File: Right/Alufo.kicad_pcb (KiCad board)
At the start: 2 copper layers, 139.7 x 88.9 mm, 72 parts, among them J2 USB_C_Receptacle_USB2.0_16P_2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, J4 USB_C_Receptacle_USB2.0_16P_2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, K11 PG1350, K12 PG1350, K13 PG1350, K14 PG1350, K15 PG1350, K16 PG1350, K21 PG1350, K22 PG1350, K23 PG1350, K24 PG1350, K25 PG1350, K26 PG1350, K31 PG1350, K32 PG1350, K33 PG1350, K34 PG1350, K41 PG1350_1½U, K42 PG1350/SKQUCAA010, SW10 BOOT, U2 CH552T, U4 USBLC6-2P6, U6 USBLC6-2P6

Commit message: Update logo and add to PCB
Logo now has PCB revision included and is positioned at top left/right edge ±1.25,+1.25mm.
Author is now positioned between lowest row 2 pad 2 and bottom edge, centred to logo.
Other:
- board text added: "${AUTHOR}"
- board text removed: "${PROJECTNAME} v${PCB_REVISION} • ${AUTHOR}"

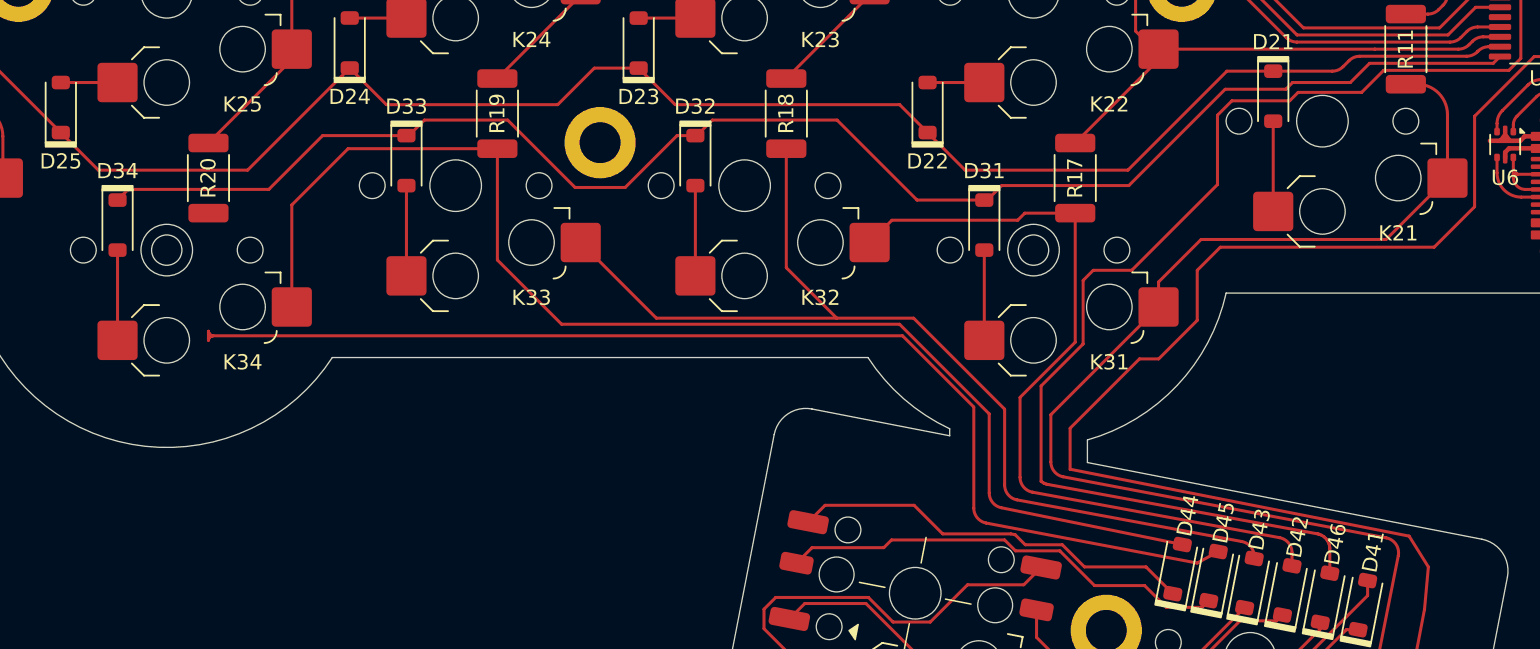
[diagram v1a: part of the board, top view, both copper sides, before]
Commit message: Realign columns on righthand side
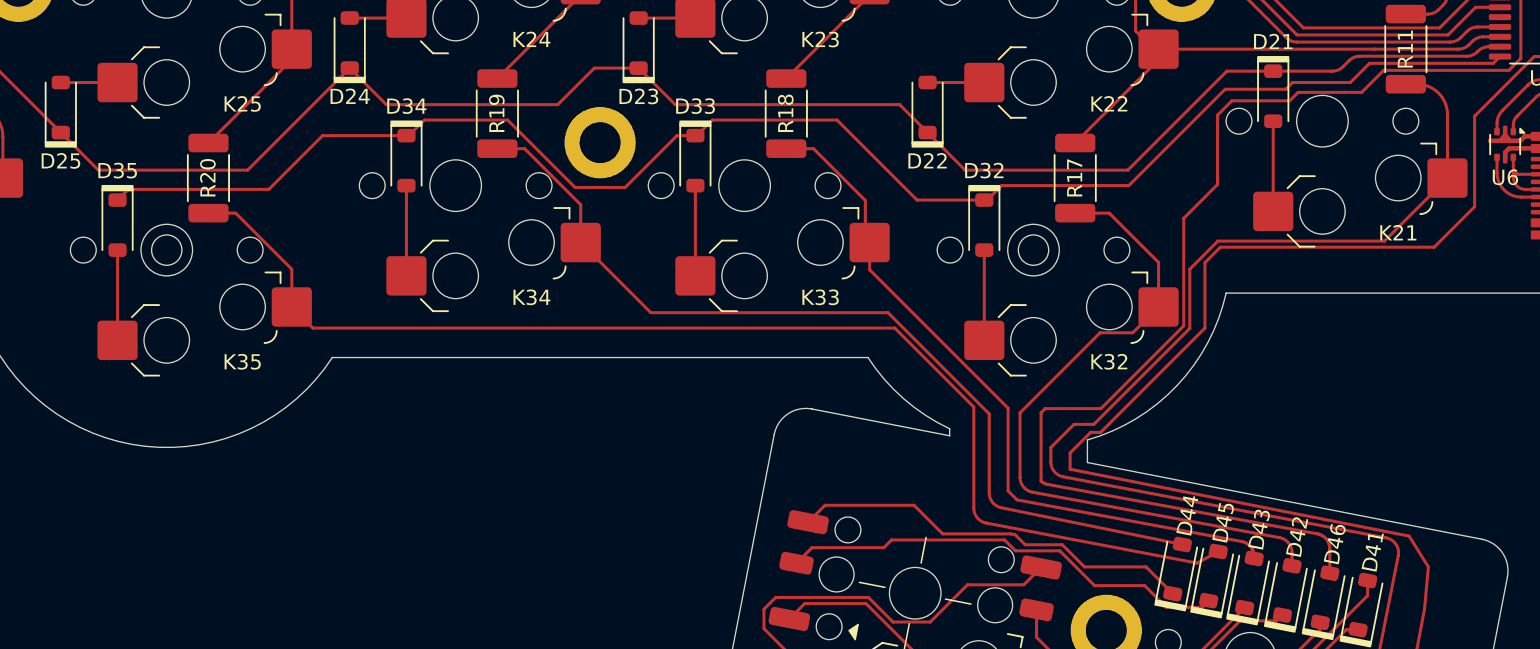
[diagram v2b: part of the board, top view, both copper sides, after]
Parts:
- renumbered D31 to D32, D32 to D33, D33 to D34, D34 to D35, K31 to K32, K32 to K33, K33 to K34, K34 to K35
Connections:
- D42 pad 2: Col2RT -> Col2T
- D43 pad 2: Col3RT -> Col3T
- D44 pad 2: Col4RT -> Col4T
- K32 pad 1: Col1T -> Col2T
- K33 pad 1: Col2RT -> Col3T
- K34 pad 1: Col3RT -> Col4T
- K35 pad 1: Col4RT -> Col5T
- R17 pad 2: Col2RT -> Col2T
- R18 pad 2: Col3RT -> Col3T
- R19 pad 2: Col4RT -> Col4T
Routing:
- net Col4RT: track 84.5 -> 0.00 mm
- net Col3RT: track 67.8 -> 0.00 mm
- net Col4T: track 0.00 -> 59.9 mm
- net Col2RT: track 53.4 -> 0.00 mm
- net Col3T: track 0.00 -> 46.6 mm
- net Col2T: track 0.00 -> 46.2 mm
- net Col5T: track 76.2 -> 81.0 mm
- net Col6: track 208.4 -> 209.1 mm

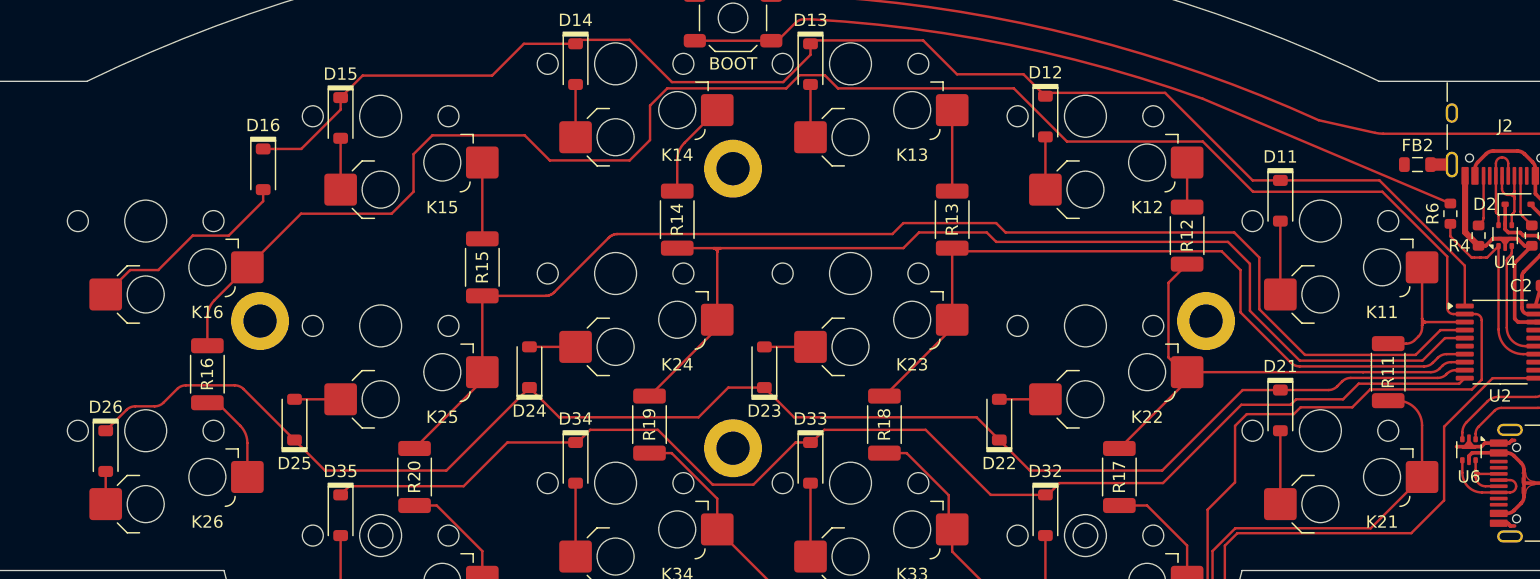
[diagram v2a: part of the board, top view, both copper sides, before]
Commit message: Remove unneeded R16 from righthand side
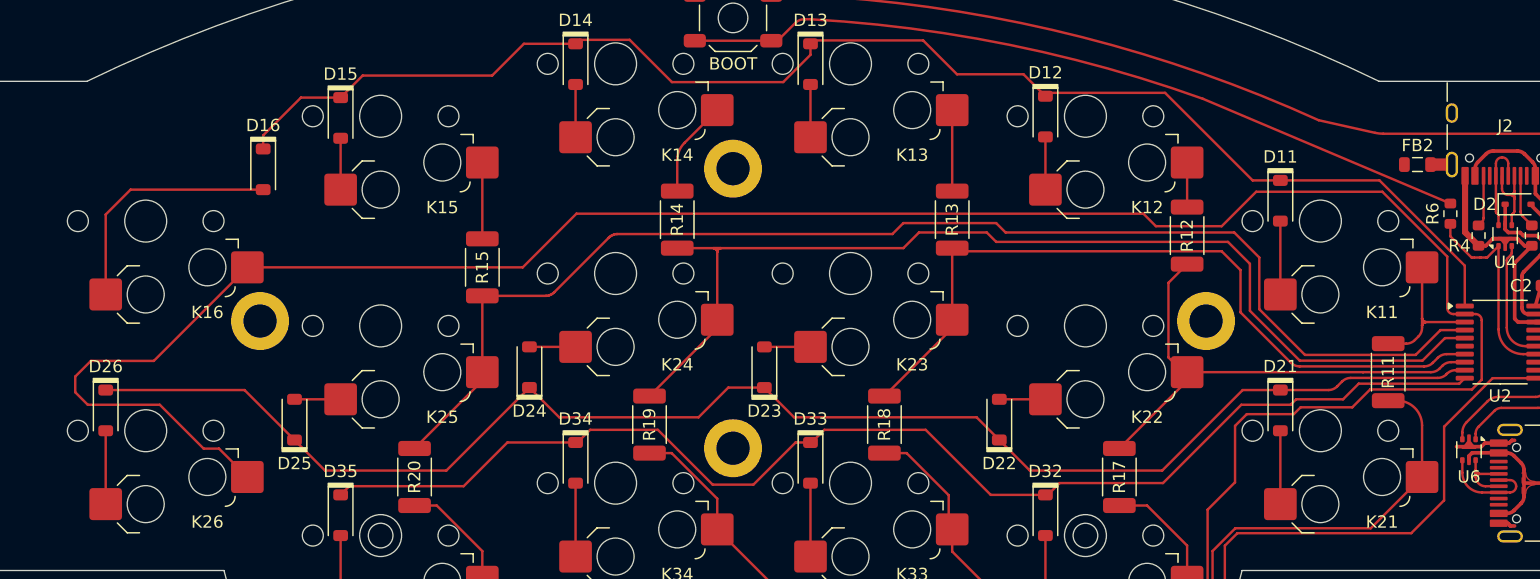
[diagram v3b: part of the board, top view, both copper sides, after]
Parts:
- removed R16: 0R, Project Library:R_2010_5025Metric_Mod
- moved D26 3.30 mm to (101.5, 67.8)
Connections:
- K26 pad 1: Col6T -> Col6
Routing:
- net Col6: track 209.1 -> 225.1 mm
- net Col6T: track 6.94 -> 0.00 mm
- net Net-(D26-A): track 2.65 -> 5.95 mm
- net Net-(D16-A): track 16.8 -> 20.1 mm
- net Row2: track 125.1 -> 123.7 mm

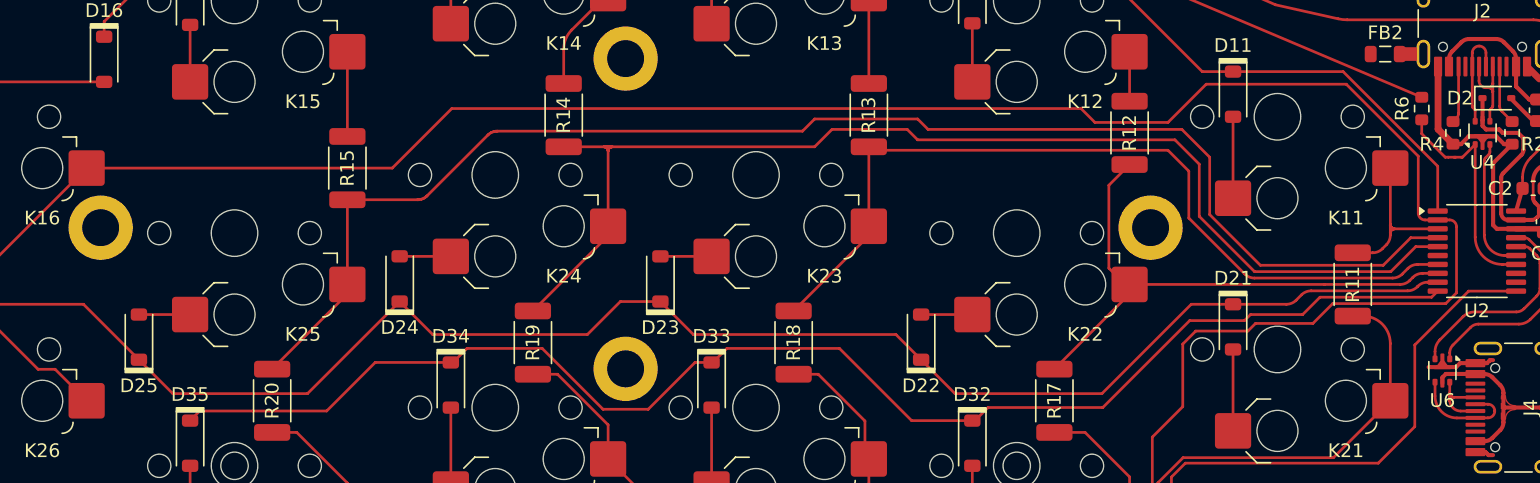
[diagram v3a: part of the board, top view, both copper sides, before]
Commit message: Route Row 2 under upper 0Ω resistors
TODO: Reconnect Column 6 to thumb row
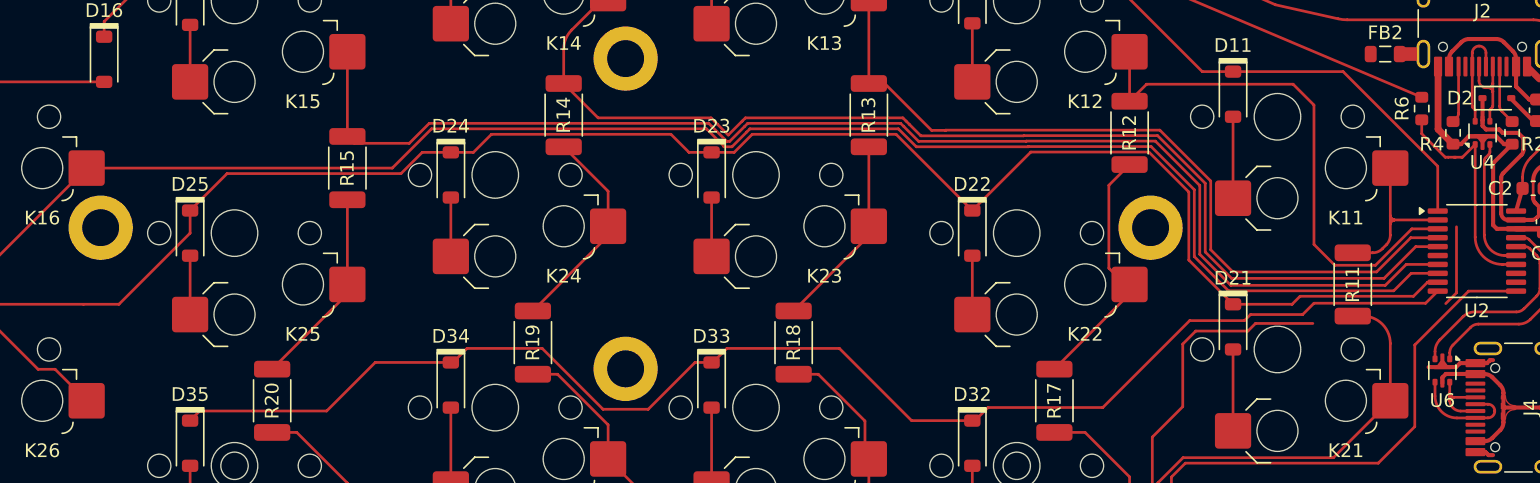
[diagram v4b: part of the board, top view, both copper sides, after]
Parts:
- moved D25 8.47 mm to (120.6, 60.9), turned to -90 degrees
- moved D22 8.47 mm to (177.7, 60.9), turned to -90 degrees
- moved D23 8.47 mm to (158.7, 56.7), turned to -90 degrees
- moved D24 8.47 mm to (139.6, 56.7), turned to -90 degrees
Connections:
- net Row4R renamed Row4
- K12 pad 1: Col2L -> Col2
- K13 pad 1: Col3L -> Col3
- K14 pad 1: Col4L -> Col4
- K15 pad 1: Col5L -> Col5
- K22 pad 1: Col2R -> Net-(K22-Pad1)
- K23 pad 1: Col3R -> Net-(K23-Pad1)
- K24 pad 1: Col4R -> Net-(K24-Pad1)
- K25 pad 1: Col5R -> Net-(K25-Pad1)
- R12 pad 1: Col2L -> Col2
- R12 pad 2: Col2R -> Net-(K22-Pad1)
- R13 pad 1: Col3L -> Col3
- R13 pad 2: Col3R -> Net-(K23-Pad1)
- R14 pad 1: Col4L -> Col4
- R14 pad 2: Col4R -> Net-(K24-Pad1)
- R15 pad 1: Col5L -> Col5
- R15 pad 2: Col5R -> Net-(K25-Pad1)
- R17 pad 1: Col2R -> Net-(K22-Pad1)
- R18 pad 1: Col3R -> Net-(K23-Pad1)
- R19 pad 1: Col4R -> Net-(K24-Pad1)
- R20 pad 1: Col5R -> Net-(K25-Pad1)
- U2 pad 2: Col6 -> Col1
- U2 pad 3: Col1 -> Col2
- U2 pad 4: Col5R -> Col3
- U2 pad 5: Col4R -> Col4
- U2 pad 7: Col3R -> Col5
- U2 pad 8: Col2R -> Col6
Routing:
- net Col5R: track 103.7 -> 0.00 mm
- net Col5: track 0.00 -> 96.2 mm
- net Col4R: track 85.2 -> 0.00 mm
- net Col4: track 0.00 -> 82.5 mm
- net Col3R: track 61.0 -> 0.00 mm
- net Col3: track 0.00 -> 57.8 mm
- net Col2R: track 40.9 -> 0.00 mm
- net Col2: track 0.00 -> 39.2 mm
- net Net-(K22-Pad1): track 0.00 -> 18.1 mm
- net Net-(K24-Pad1): track 0.00 -> 14.9 mm
- net Net-(K25-Pad1): track 0.00 -> 14.0 mm
- net Net-(K23-Pad1): track 0.00 -> 13.6 mm
- net Col6: track 225.1 -> 213.8 mm
- net Col4L: track 7.82 -> 0.00 mm
- net Col3L: track 6.57 -> 0.00 mm
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
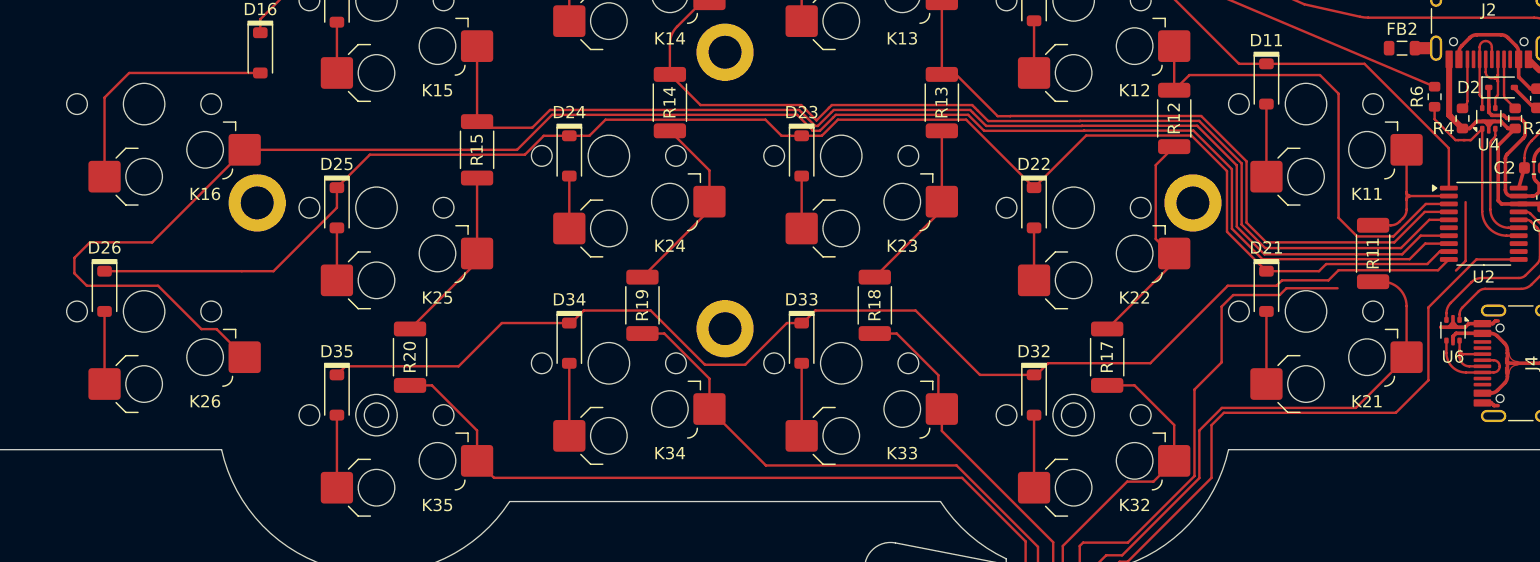
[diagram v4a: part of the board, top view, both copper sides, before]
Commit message: Route Row 3 under upper 0Ω resistors and remove lower 0Ω resistors
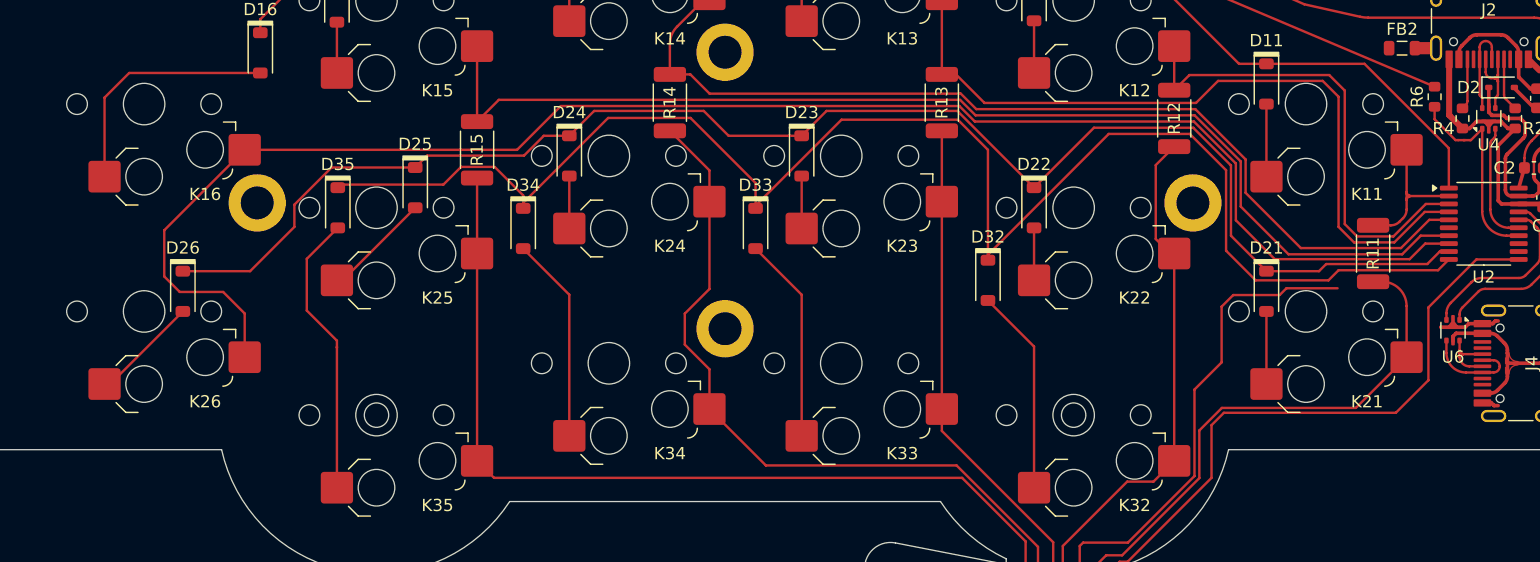
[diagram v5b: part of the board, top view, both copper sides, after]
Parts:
- removed R17, R18, R19, R20: 0R, Project Library:R_2010_5025Metric_Mod
- moved D35 15.4 mm to (120.7, 60.9)
- moved D32 10.1 mm to (173.9, 66.9)
- moved D33 10.1 mm to (154.9, 62.6)
- moved D34 10.1 mm to (135.8, 62.6)
- moved D25 6.63 mm to (127.0, 59.3)
- moved D26 6.42 mm to (108.0, 67.8)
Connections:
- K22 pad 1: Net-(K22-Pad1) -> Col2T
- K23 pad 1: Net-(K23-Pad1) -> Col3T
- K24 pad 1: Net-(K24-Pad1) -> Col4T
- K25 pad 1: Net-(K25-Pad1) -> Col5T
- R12 pad 2: Net-(K22-Pad1) -> Col2T
- R13 pad 2: Net-(K23-Pad1) -> Col3T
- R14 pad 2: Net-(K24-Pad1) -> Col4T
- R15 pad 2: Net-(K25-Pad1) -> Col5T
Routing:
- net Row3: track 102.6 -> 128.8 mm
- net Net-(K22-Pad1): track 18.1 -> 0.00 mm
- net Col6: track 213.8 -> 196.0 mm
- net Col2T: track 46.2 -> 63.8 mm
- net Net-(D35-A): track 5.95 -> 23.5 mm
- net Col4T: track 59.9 -> 76.2 mm
- net Net-(K24-Pad1): track 14.9 -> 0.00 mm
- net Net-(K25-Pad1): track 14.0 -> 0.00 mm
- net Col3T: track 46.6 -> 60.3 mm
- net Col5T: track 81.0 -> 94.7 mm
- net Net-(K23-Pad1): track 13.6 -> 0.00 mm
- net Net-(D34-A): track 5.95 -> 16.9 mm
- net Net-(D33-A): track 5.95 -> 16.9 mm
- net Net-(D32-A): track 5.95 -> 16.9 mm
- net Col3: track 57.8 -> 62.6 mm
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
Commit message: Relocate diodes
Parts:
- moved D35 15.4 mm to (120.6, 76.3)
- moved D16 13.4 mm to (101.5, 52.4)
- moved D32 10.1 mm to (177.7, 76.3)
- moved D33 10.1 mm to (158.7, 72.0)
- moved D34 10.1 mm to (139.6, 72.0)
- moved D26 6.63 mm to (101.5, 69.4)
- moved D25 6.42 mm to (120.6, 59.3)
- moved R14 3.81 mm to (151.1, 54.3)
- moved R13 1.99 mm to (170.2, 54.3)
- moved R15 1.88 mm to (132.1, 54.3)
- moved D22 1.65 mm to (177.7, 59.3)
- moved R12 0.70 mm to (189.2, 54.3)
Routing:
- net Col6: track 196.0 -> 249.1 mm
- net Row3: track 128.8 -> 176.8 mm
- net Net-(D35-A): track 23.5 -> 5.95 mm
- net Net-(D16-A): track 20.1 -> 4.30 mm
- net Row1: track 114.9 -> 129.1 mm
- net Net-(D34-A): track 16.9 -> 5.95 mm
- net Net-(D33-A): track 16.9 -> 5.95 mm
- net Net-(D32-A): track 16.9 -> 5.95 mm
- net Net-(D26-A): track 8.88 -> 4.30 mm
- net Row2: track 125.5 -> 129.9 mm
- net Col4T: track 76.2 -> 72.8 mm
- net Net-(D25-A): track 8.88 -> 5.95 mm
- net Col5: track 94.6 -> 92.1 mm
- net Col3T: track 60.3 -> 58.2 mm
- net Col3: track 62.6 -> 64.6 mm
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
